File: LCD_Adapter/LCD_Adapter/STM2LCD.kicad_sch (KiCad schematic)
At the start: 17 parts, among them J1 Conn_01x10, J2 FH12-30S-0.5SH_55_, J6 2-1734248-0

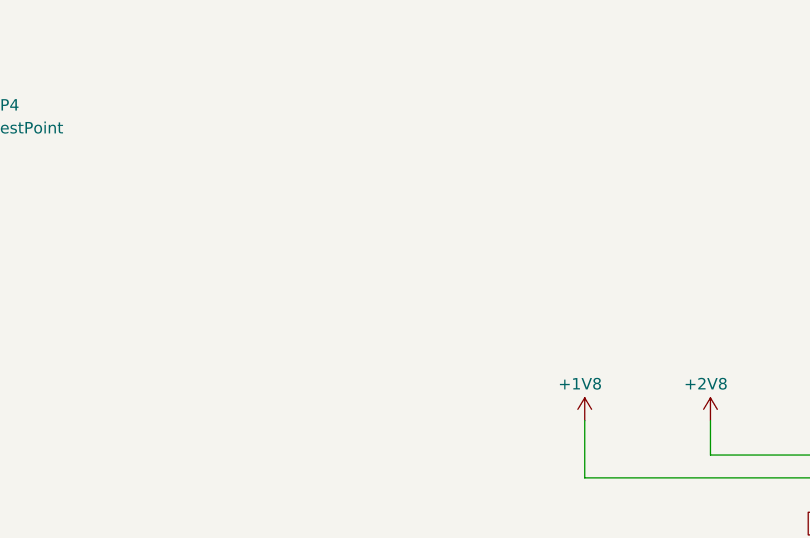
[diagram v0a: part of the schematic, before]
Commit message: adapter board done. ordered
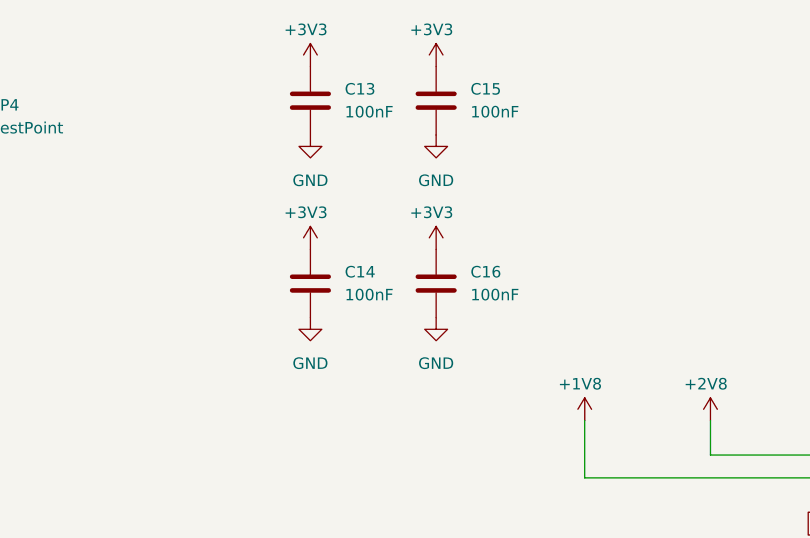
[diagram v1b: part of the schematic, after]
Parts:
- added C13, C14, C15, C16: 100nF, Capacitor_SMD:C_0402_1005Metric, symbol Device:C
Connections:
- net +3V3: now also C13.1, C14.1, C15.1, C16.1
- net GND: now also C13.2, C14.2, C15.2, C16.2
